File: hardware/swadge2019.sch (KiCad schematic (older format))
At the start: 48 parts, among them P1 PGM, P10 CONN_1, P11 CONN_1, P12 CONN_1, P13 CONN_1, P2 USBMicroB-10118192-0001LF, P3 SAO, P4 CONN_1, P6 CONN_1, P7 CONN_1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

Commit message: update design
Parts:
- C1: value 10u -> 22u
- R11, R9: value 1.5k -> NP_1k
- R3: value 22k -> 10k
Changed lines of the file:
@@
 P 7000 3150
 F 0 "C1" H 7025 3250 50  0000 L CNN
-F 1 "10u" H 7025 3050 50  0000 L CNN
+F 1 "22u" H 7025 3050 50  0000 L CNN
 F 2 "C_0805" H 7038 3000 50  0000 C CNN
 F 3 "" H 7000 3150 50  0000 C CNN
@@
 P 1700 2050
 F 0 "R3" V 1780 2050 50  0000 C CNN
-F 1 "22k" V 1700 2050 50  0000 C CNN
+F 1 "10k" V 1700 2050 50  0000 C CNN
 F 2 "R_0805" V 1630 2050 50  0000 C CNN
 F 3 "" H 1700 2050 50  0000 C CNN
@@
 P 6650 3800
 F 0 "R9" V 6730 3800 50  0000 C CNN
-F 1 "1.5k" V 6650 3800 50  0000 C CNN
+F 1 "NP_1k" V 6650 3800 50  0000 C CNN
 F 2 "R_0805" V 6580 3800 50  0000 C CNN
 F 3 "" H 6650 3800 50  0000 C CNN
@@
 P 7000 3800
 F 0 "R11" V 7080 3800 50  0000 C CNN
-F 1 "1.5k" V 7000 3800 50  0000 C CNN
+F 1 "NP_1k" V 7000 3800 50  0000 C CNN
 F 2 "R_0805" V 6930 3800 50  0000 C CNN
 F 3 "" H 7000 3800 50  0000 C CNN

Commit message: Add RevD
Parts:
- C2: value 1u -> .22u
- C4, C5, C6, C7, C8: value .1u -> .22u
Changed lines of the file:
@@
 P 1050 2350
 F 0 "C2" H 1075 2450 50  0000 L CNN
-F 1 "1u" H 1075 2250 50  0000 L CNN
+F 1 ".22u" H 1075 2250 50  0000 L CNN
 F 2 "C_0805" H 1088 2200 50  0000 C CNN
 F 3 "" H 1050 2350 50  0000 C CNN
@@
 P 7350 3150
 F 0 "C4" H 7375 3250 50  0000 L CNN
-F 1 ".1u" H 7375 3050 50  0000 L CNN
+F 1 ".22u" H 7375 3050 50  0000 L CNN
 F 2 "C_0805" H 7388 3000 50  0000 C CNN
 F 3 "" H 7350 3150 50  0000 C CNN
@@
 P 7750 3150
 F 0 "C5" H 7775 3250 50  0000 L CNN
-F 1 ".1u" H 7775 3050 50  0000 L CNN
+F 1 ".22u" H 7775 3050 50  0000 L CNN
 F 2 "C_0805" H 7788 3000 50  0000 C CNN
 F 3 "" H 7750 3150 50  0000 C CNN
@@
 P 6550 3150
 F 0 "C6" H 6575 3250 50  0000 L CNN
-F 1 ".1u" H 6575 3050 50  0000 L CNN
+F 1 ".22u" H 6575 3050 50  0000 L CNN
 F 2 "C_0805" H 6588 3000 50  0000 C CNN
 F 3 "" H 6550 3150 50  0000 C CNN
@@
 P 1250 3050
 F 0 "C7" H 1275 3150 50  0000 L CNN
-F 1 ".1u" H 1275 2950 50  0000 L CNN
+F 1 ".22u" H 1275 2950 50  0000 L CNN
 F 2 "C_0805" H 1288 2900 50  0000 C CNN
 F 3 "" H 1250 3050 50  0000 C CNN
@@
 P 8050 2550
 F 0 "C8" H 8075 2650 50  0000 L CNN
-F 1 ".1u" H 8075 2450 50  0000 L CNN
+F 1 ".22u" H 8075 2450 50  0000 L CNN
 F 2 "C_0805" H 8088 2400 50  0000 C CNN
 F 3 "" H 8050 2550 50  0000 C CNN

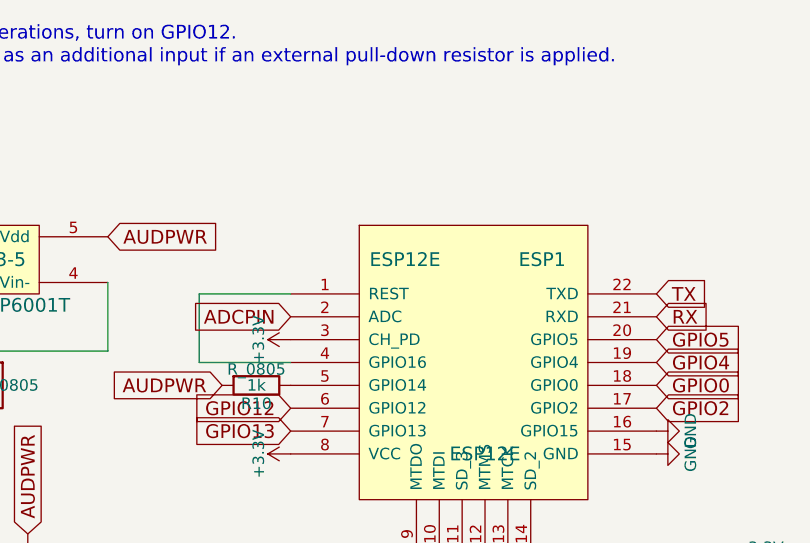
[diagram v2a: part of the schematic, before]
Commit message: Update labels and RFQ
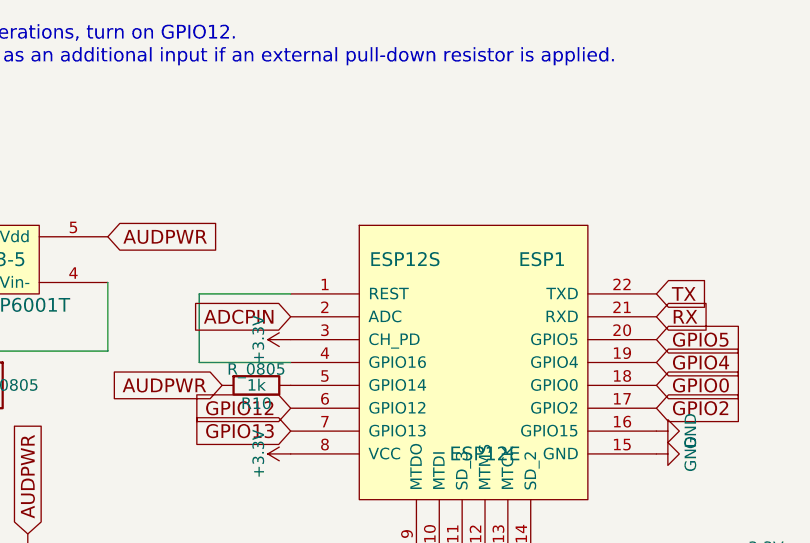
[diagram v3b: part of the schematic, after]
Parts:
- BT1, BT2: MFG (none) -> Use through-hole AA Battery Holder in Style of Keystone 2460
- D3: MFG (none) -> MUST use OFFICIAL SK6812-SIDE LEDs.
- ESP1: value ESP12E -> ESP12S; MFG (none) -> N/A Use ESP12S or ESP12F Modules from Electrodragon
- P2: MFG (none) -> Must use micro USB SMT-only Header, like 10118192-0001LF
- P3: MFG (none) -> Do not populate
- R11, R2, R9: MFG (none) -> Do Not Populate
- SW2: MFG (none) -> Use standard SMT box tactile buttons. Similar to PTS645SM43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
- SW3: Digikey https://www.aliexpress.com/item/50pcs-lot-SMT-3x6x2-5MM-2PI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 -> (none); MFG (none) -> https://www.aliexpress.com/item/50pcs-lot-SMT-3x6x2-5MM-2PI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
- SW7: Cost100 0.48010 -> (none); Digikey 401-1999-6-ND -> (none); MFG (none) -> Use SPDT SLID Switch, like 401-1999-6-ND
- U1: MFG (none) -> Must use MCP6001T Opamp
- U2: MFG (none) -> Use any 1117 3.3V SOT-223 regulator. I.e. AZ1117 or AP1117
- Y1: MFG (none) -> Use a standard through-hole electret microphone.
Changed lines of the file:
@@
 P 3950 2250
 F 0 "ESP1" H 4250 2850 60  0000 C CNN
-F 1 "ESP12E" H 3650 2850 60  0000 C CNN
+F 1 "ESP12S" H 3650 2850 60  0000 C CNN
 F 2 "ESP12E" H 4000 2000 60  0000 C CNN
 F 3 "" H 4000 2000 60  0000 C CNN
+F 4 "N/A Use ESP12S or ESP12F Modules from Electrodragon" H 3950 2250 60  0001 C CNN "MFG"
 	1    3950 2250
 	1    0    0    -1
@@
 F 2 "TACTILE10" H 7350 2100 60  0000 C CNN
 F 3 "" H 7350 2100 60  0000 C CNN
+F 4 "Use standard SMT box tactile buttons.  Similar to PTS645SM43SMTR92. Use RoHS if possible." H 7350 2100 60  0001 C CNN "MFG"
 	1    7350 2100
 	1    0    0    -1
@@
 F 2 "SOT-23-5" H 1800 1650 60  0000 C CNN
 F 3 "" H 1800 1650 60  0000 C CNN
+F 4 "Must use MCP6001T Opamp" H 1800 1650 60  0001 C CNN "MFG"
 	1    1800 1650
 	1    0    0    -1
@@
 F 2 "C_Radial_D8_L13_P3.8" H 700 2550 50  0000 C CNN
 F 3 "" H 800 2800 50  0000 C CNN
+F 4 "Use a standard through-hole electret microphone." H 800 2800 60  0001 C CNN "MFG"
 	1    800  2800
 	0    1    1    0
@@
 F 2 "R_0805" V 5730 3200 50  0000 C CNN
 F 3 "" H 5800 3200 50  0000 C CNN
+F 4 "Do Not Populate" V 5800 3200 60  0001 C CNN "MFG"
 	1    5800 3200
 	1    0    0    -1
@@
 F 2 "SK6812SIDE" H 4700 5350 60  0000 C CNN
 F 3 "" H 4700 5350 60  0000 C CNN
+F 4 "MUST use OFFICIAL SK6812-SIDE LEDs.  " H 4700 5350 60  0001 C CNN "MFG"
 	1    4700 5350
 	1    0    0    -1
@@
 F 2 "USBMicroB-10118192-0001LF" H 7650 4550 60  0001 C CNN
 F 3 "" H 7650 4550 60  0001 C CNN
+F 4 "Must use micro USB SMT-only Header, like 10118192-0001LF" H 7650 4500 60  0001 C CNN "MFG"
 	1    7650 4500
 	1    0    0    -1
@@
 F 2 "JS_SWITCH" H 8800 3300 50  0000 C CNN
 F 3 "" H 8800 3300 50  0000 C CNN
-F 4 "401-1999-6-ND" H 8800 3300 60  0001 C CNN "Digikey"
-F 5 "0.48010" H 8800 3300 60  0001 C CNN "Cost100"
+F 4 "Use SPDT SLID Switch, like 401-1999-6-ND" H 8800 3300 60  0001 C CNN "MFG"
 	1    8800 3300
 	1    0    0    -1
@@
 F 2 "SOT-223" H 9350 4350 60  0000 C CNN
 F 3 "" H 9350 4350 60  0000 C CNN
+F 4 "Use any 1117 3.3V SOT-223 regulator.  I.e. AZ1117 or AP1117" H 9350 4350 60  0001 C CNN "MFG"
 	1    9350 4350
 	1    0    0    -1
@@
 F 2 "BCAAPC" V 10050 3040 50  0000 C CNN
 F 3 "" V 10050 3040 50  0000 C CNN
+F 4 "Use through-hole AA Battery Holder in Style of Keystone 2460" H 10050 3000 60  0001 C CNN "MFG"
 	1    10050 3000
 	1    0    0    -1
@@
 F 2 "BCAAPC" V 10050 3340 50  0000 C CNN
 F 3 "" V 10050 3340 50  0000 C CNN
+F 4 "Use through-hole AA Battery Holder in Style of Keystone 2460" H 10050 3300 60  0001 C CNN "MFG"
 	1    10050 3300
 	1    0    0    -1
@@
 F 2 "R_0805" V 6580 3800 50  0000 C CNN
 F 3 "" H 6650 3800 50  0000 C CNN
+F 4 "Do Not Populate" V 6650 3800 60  0001 C CNN "MFG"
 	1    6650 3800
 	1    0    0    -1
@@
 F 2 "Pin_Header_Straight_2x02" H 7500 5100 50  0000 C CNN
 F 3 "" H 7500 4150 50  0000 C CNN
+F 4 "Do not populate" H 7500 5350 60  0001 C CNN "MFG"
 	1    7500 5350
 	1    0    0    -1
@@
 F 2 "R_0805" V 6930 3800 50  0000 C CNN
 F 3 "" H 7000 3800 50  0000 C CNN
+F 4 "Do Not Populate" V 7000 3800 60  0001 C CNN "MFG"
 	1    7000 3800
 	1    0    0    -1
@@
 F 2 "TACT_3x6_SINGLE" H 7400 1150 50  0000 C CNN
 F 3 "" H 7400 1150 50  0000 C CNN
-F 4 "https://www.aliexpress.com/item/50pcs-lot-SMT-3x6x2-5MM-2PIN-Tactile-Tact-Push-Button-Micro-Switch-G73-Self-reset-Momentary/32804523270.html?spm=2114.search0104.3.65.6bbc193exM3dfC&ws_ab_test=searchweb0_0,searchweb201602_3_10065_10068_10130_318_10547_319_10546_317_10548_10545_10696_450_10084_10083_10618_452_535_534_533_10307_532_204_10059_10884_10887_100031_320_10103_448_449,searchweb201603_60,ppcSwitch_0&algo_expid=b407050b-5903-45ff-9783-15a47ce9142d-9&algo_pvid=b407050b-5903-45ff-9783-15a47ce9142d&priceBeautifyAB=0" H 7400 1150 60  0001 C CNN "Digikey"
+F 4 "https://www.aliexpress.com/item/50pcs-lot-SMT-3x6x2-5MM-2PIN-Tactile-Tact-Push-Button-Micro-Switch-G73-Self-reset-Momentary/32804523270.html?spm=2114.search0104.3.65.6bbc193exM3dfC&ws_ab_test=searchweb0_0,searchweb201602_3_10065_10068_10130_318_10547_319_10546_317_10548_10545_10696_450_10084_10083_10618_452_535_534_533_10307_532_204_10059_10884_10887_100031_320_10103_448_449,searchweb201603_60,ppcSwitch_0&algo_expid=b407050b-5903-45ff-9783-15a47ce9142d-9&algo_pvid=b407050b-5903-45ff-9783-15a47ce9142d&priceBeautifyAB=0" H 7400 1150 60  0001 C CNN "MFG"
 	1    7400 1150
 	1    0    0    -1

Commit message: Update rev with better microphone support
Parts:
- added Y2: Mic, 6mmELECTRET_MIC_SMT, symbol Crystal
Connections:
- net GND: now also Y2.2
- net at C2.2, R6.2, Y1.1: now also Y2.1
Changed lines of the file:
@@
 $EndComp
 $Comp
-L GND #PWR52
+L GND #PWR53
 U 1 1 5B9496E7
 P 3450 5500
-F 0 "#PWR52" H 3450 5250 50  0001 C CNN
+F 0 "#PWR53" H 3450 5250 50  0001 C CNN
 F 1 "GND" H 3450 5350 50  0000 C CNN
 F 2 "" H 3450 5500 50  0000 C CNN
@@
 $EndComp
 $Comp
-L GND #PWR53
+L GND #PWR54
 U 1 1 5B9497A7
 P 4500 5500
-F 0 "#PWR53" H 4500 5250 50  0001 C CNN
+F 0 "#PWR54" H 4500 5250 50  0001 C CNN
 F 1 "GND" H 4500 5350 50  0000 C CNN
 F 2 "" H 4500 5500 50  0000 C CNN
@@
 $EndComp
 $Comp
-L GND #PWR58
+L GND #PWR59
 U 1 1 5B94997F
 P 3450 6400
-F 0 "#PWR58" H 3450 6150 50  0001 C CNN
+F 0 "#PWR59" H 3450 6150 50  0001 C CNN
 F 1 "GND" H 3450 6250 50  0000 C CNN
 F 2 "" H 3450 6400 50  0000 C CNN
@@
 $EndComp
 $Comp
-L GND #PWR59
+L GND #PWR60
 U 1 1 5B949991
 P 4500 6400
-F 0 "#PWR59" H 4500 6150 50  0001 C CNN
+F 0 "#PWR60" H 4500 6150 50  0001 C CNN
 F 1 "GND" H 4500 6250 50  0000 C CNN
 F 2 "" H 4500 6400 50  0000 C CNN
@@
 $EndComp
 $Comp
-L GND #PWR51
+L GND #PWR52
 U 1 1 5B949C6D
 P 2500 5500
-F 0 "#PWR51" H 2500 5250 50  0001 C CNN
+F 0 "#PWR52" H 2500 5250 50  0001 C CNN
 F 1 "GND" H 2500 5350 50  0000 C CNN
 F 2 "" H 2500 5500 50  0000 C CNN
@@
 	800  2450 800  2650
 Wire Wire Line
-	800  2550 1050 2550
+	800  2550 1100 2550
 Wire Wire Line
 	1050 2550 1050 2500
@@
 	2100 6300 2500 6300
 $Comp
-L GND #PWR57
+L GND #PWR58
 U 1 1 5B949FA9
 P 2500 6400
-F 0 "#PWR57" H 2500 6150 50  0001 C CNN
+F 0 "#PWR58" H 2500 6150 50  0001 C CNN
 F 1 "GND" H 2500 6250 50  0000 C CNN
 F 2 "" H 2500 6400 50  0000 C CNN
@@
 $EndComp
 $Comp
-L GND #PWR42
+L GND #PWR43
 U 1 1 5B94A9A3
 P 7600 4800
-F 0 "#PWR42" H 7600 4550 50  0001 C CNN
+F 0 "#PWR43" H 7600 4550 50  0001 C CNN
 F 1 "GND" H 7600 4650 50  0000 C CNN
 F 2 "" H 7600 4800 50  0000 C CNN
@@
 $EndComp
 $Comp
-L GND #PWR43
+L GND #PWR44
 U 1 1 5B94AA02
 P 7700 4800
-F 0 "#PWR43" H 7700 4550 50  0001 C CNN
+F 0 "#PWR44" H 7700 4550 50  0001 C CNN
 F 1 "GND" H 7700 4650 50  0000 C CNN
 F 2 "" H 7700 4800 50  0000 C CNN
@@
 $EndComp
 $Comp
-L GND #PWR44
+L GND #PWR45
 U 1 1 5B94AA61
 P 7800 4800
-F 0 "#PWR44" H 7800 4550 50  0001 C CNN
+F 0 "#PWR45" H 7800 4550 50  0001 C CNN
 F 1 "GND" H 7800 4650 50  0000 C CNN
 F 2 "" H 7800 4800 50  0000 C CNN
@@
 $EndComp
 $Comp
-L GND #PWR45
+L GND #PWR46
 U 1 1 5B94AAC0
 P 7900 4800
-F 0 "#PWR45" H 7900 4550 50  0001 C CNN
+F 0 "#PWR46" H 7900 4550 50  0001 C CNN
 F 1 "GND" H 7900 4650 50  0000 C CNN
 F 2 "" H 7900 4800 50  0000 C CNN
@@
 $EndComp
 $Comp
-L GND #PWR41
+L GND #PWR42
 U 1 1 5B94AB1F
 P 7150 4700
-F 0 "#PWR41" H 7150 4450 50  0001 C CNN
+F 0 "#PWR42" H 7150 4450 50  0001 C CNN
 F 1 "GND" H 7150 4550 50  0000 C CNN
 F 2 "" H 7150 4700 50  0000 C CNN
@@
 $EndComp
 $Comp
-L +5V #PWR37
+L +5V #PWR38
 U 1 1 5B94B2D2
 P 7150 4300
-F 0 "#PWR37" H 7150 4150 50  0001 C CNN
+F 0 "#PWR38" H 7150 4150 50  0001 C CNN
 F 1 "+5V" H 7150 4440 50  0000 C CNN
 F 2 "" H 7150 4300 50  0000 C CNN
@@
 $EndComp
 $Comp
-L GND #PWR39
+L GND #PWR40
 U 1 1 5B94BF15
 P 9900 4450
-F 0 "#PWR39" H 9900 4200 50  0001 C CNN
+F 0 "#PWR40" H 9900 4200 50  0001 C CNN
 F 1 "GND" H 9900 4300 50  0000 C CNN
 F 2 "" H 9900 4450 50  0000 C CNN
@@
 $EndComp
 $Comp
-L +3.3V #PWR54
+L +3.3V #PWR55
 U 1 1 5B94C316
 P 2500 6200
-F 0 "#PWR54" H 2500 6050 50  0001 C CNN
+F 0 "#PWR55" H 2500 6050 50  0001 C CNN
 F 1 "+3.3V" H 2500 6340 50  0000 C CNN
 F 2 "" H 2500 6200 50  0000 C CNN
@@
 $EndComp
 $Comp
-L +3.3V #PWR46
+L +3.3V #PWR47
 U 1 1 5B94C4CF
 P 2500 5300
-F 0 "#PWR46" H 2500 5150 50  0001 C CNN
+F 0 "#PWR47" H 2500 5150 50  0001 C CNN
 F 1 "+3.3V" H 2500 5440 50  0000 C CNN
 F 2 "" H 2500 5300 50  0000 C CNN
@@
 $EndComp
 $Comp
-L +3.3V #PWR47
+L +3.3V #PWR48
 U 1 1 5B94CBC4
 P 3450 5300
-F 0 "#PWR47" H 3450 5150 50  0001 C CNN
+F 0 "#PWR48" H 3450 5150 50  0001 C CNN
 F 1 "+3.3V" H 3450 5440 50  0000 C CNN
 F 2 "" H 3450 5300 50  0000 C CNN
@@
 $EndComp
 $Comp
-L +3.3V #PWR55
+L +3.3V #PWR56
 U 1 1 5B94CC29
 P 3450 6200
-F 0 "#PWR55" H 3450 6050 50  0001 C CNN
+F 0 "#PWR56" H 3450 6050 50  0001 C CNN
 F 1 "+3.3V" H 3450 6340 50  0000 C CNN
 F 2 "" H 3450 6200 50  0000 C CNN
@@
 $EndComp
 $Comp
-L +3.3V #PWR56
+L +3.3V #PWR57
 U 1 1 5B94CC8E
 P 4500 6200
-F 0 "#PWR56" H 4500 6050 50  0001 C CNN
+F 0 "#PWR57" H 4500 6050 50  0001 C CNN
 F 1 "+3.3V" H 4500 6340 50  0000 C CNN
 F 2 "" H 4500 6200 50  0000 C CNN
@@
 $EndComp
 $Comp
-L +3.3V #PWR48
+L +3.3V #PWR49
 U 1 1 5B94CCF3
 P 4500 5300
-F 0 "#PWR48" H 4500 5150 50  0001 C CNN
+F 0 "#PWR49" H 4500 5150 50  0001 C CNN
 F 1 "+3.3V" H 4500 5440 50  0000 C CNN
 F 2 "" H 4500 5300 50  0000 C CNN
@@
 $EndComp
 $Comp
-L +5V #PWR36
+L +5V #PWR37
 U 1 1 5B94D2F0
 P 9900 4250
-F 0 "#PWR36" H 9900 4100 50  0001 C CNN
+F 0 "#PWR37" H 9900 4100 50  0001 C CNN
 F 1 "+5V" H 9900 4390 50  0000 C CNN
 F 2 "" H 9900 4250 50  0000 C CNN
@@
 $EndComp
 $Comp
-L GND #PWR32
+L GND #PWR33
 U 1 1 5B94B42A
 P 5650 3750
-F 0 "#PWR32" H 5650 3500 50  0001 C CNN
+F 0 "#PWR33" H 5650 3500 50  0001 C CNN
 F 1 "GND" H 5650 3600 50  0000 C CNN
 F 2 "" H 5650 3750 50  0000 C CNN
@@
 $EndComp
 $Comp
-L GND #PWR33
+L GND #PWR34
 U 1 1 5B94B430
 P 5650 3900
-F 0 "#PWR33" H 5650 3650 50  0001 C CNN
+F 0 "#PWR34" H 5650 3650 50  0001 C CNN
 F 1 "GND" H 5650 3750 50  0000 C CNN
 F 2 "" H 5650 3900 50  0000 C CNN
@@
 $EndComp
 $Comp
-L GND #PWR34
+L GND #PWR35
 U 1 1 5B94B436
 P 5650 4050
-F 0 "#PWR34" H 5650 3800 50  0001 C CNN
+F 0 "#PWR35" H 5650 3800 50  0001 C CNN
 F 1 "GND" H 5650 3900 50  0000 C CNN
 F 2 "" H 5650 4050 50  0000 C CNN
@@
 $EndComp
 $Comp
-L GND #PWR35
+L GND #PWR36
 U 1 1 5B94B43C
 P 5650 4200
-F 0 "#PWR35" H 5650 3950 50  0001 C CNN
+F 0 "#PWR36" H 5650 3950 50  0001 C CNN
 F 1 "GND" H 5650 4050 50  0000 C CNN
 F 2 "" H 5650 4200 50  0000 C CNN
@@
 $EndComp
 $Comp
-L GND #PWR38
+L GND #PWR39
 U 1 1 5B94B52A
 P 5650 4350
-F 0 "#PWR38" H 5650 4100 50  0001 C CNN
+F 0 "#PWR39" H 5650 4100 50  0001 C CNN
 F 1 "GND" H 5650 4200 50  0000 C CNN
 F 2 "" H 5650 4350 50  0000 C CNN
@@
 $EndComp
 $Comp
-L GND #PWR40
+L GND #PWR41
 U 1 1 5B94B530
 P 5650 4500
-F 0 "#PWR40" H 5650 4250 50  0001 C CNN
+F 0 "#PWR41" H 5650 4250 50  0001 C CNN
 F 1 "GND" H 5650 4350 50  0000 C CNN
 F 2 "" H 5650 4500 50  0000 C CNN
@@
 $EndComp
 $Comp
-L GND #PWR29
+L GND #PWR30
 U 1 1 5B94B7AB
 P 4850 3600
-F 0 "#PWR29" H 4850 3350 50  0001 C CNN
+F 0 "#PWR30" H 4850 3350 50  0001 C CNN
 F 1 "GND" H 4850 3450 50  0000 C CNN
 F 2 "" H 4850 3600 50  0000 C CNN
@@
 $EndComp
 $Comp
-L +3.3V #PWR30
+L +3.3V #PWR31
 U 1 1 5B94FABC
 P 6650 3650
-F 0 "#PWR30" H 6650 3500 50  0001 C CNN
+F 0 "#PWR31" H 6650 3500 50  0001 C CNN
 F 1 "+3.3V" H 6650 3790 50  0000 C CNN
 F 2 "" H 6650 3650 50  0000 C CNN
@@
 $EndComp
 $Comp
-L GND #PWR50
+L GND #PWR51
 U 1 1 5BC45215
 P 7750 5300
-F 0 "#PWR50" H 7750 5050 50  0001 C CNN
+F 0 "#PWR51" H 7750 5050 50  0001 C CNN
 F 1 "GND" H 7750 5150 50  0000 C CNN
 F 2 "" H 7750 5300 50  0000 C CNN
@@
 $EndComp
 $Comp
-L +3.3V #PWR49
+L +3.3V #PWR50
 U 1 1 5BC4539E
 P 7250 5300
-F 0 "#PWR49" H 7250 5150 50  0001 C CNN
+F 0 "#PWR50" H 7250 5150 50  0001 C CNN
 F 1 "+3.3V" H 7250 5440 50  0000 C CNN
 F 2 "" H 7250 5300 50  0000 C CNN
@@
 $EndComp
 $Comp
-L +3.3V #PWR31
+L +3.3V #PWR32
 U 1 1 5BC4BC3D
 P 7000 3650
-F 0 "#PWR31" H 7000 3500 50  0001 C CNN
+F 0 "#PWR32" H 7000 3500 50  0001 C CNN
 F 1 "+3.3V" H 7000 3790 50  0000 C CNN
 F 2 "" H 7000 3650 50  0000 C CNN
@@
 	-1   0    0    1
 $EndComp
+$Comp
+L Crystal Y2
+U 1 1 5BD94020
+P 800 3450
+F 0 "Y2" H 800 3600 50  0000 C CNN
+F 1 "Mic" H 800 3300 50  0000 C CNN
+F 2 "6mmELECTRET_MIC_SMT" H 700 3200 50  0000 C CNN
+F 3 "" H 800 3450 50  0000 C CNN
+F 4 "Use a standard through-hole electret microphone." H 800 3450 60  0001 C CNN "MFG"
+	1    800  3450
+	0    1    1    0
+$EndComp
+$Comp
+L GND #PWR29
+U 1 1 5BD94187
+P 800 3600
+F 0 "#PWR29" H 800 3350 50  0001 C CNN
+F 1 "GND" H 800 3450 50  0000 C CNN
+F 2 "" H 800 3600 50  0000 C CNN
+F 3 "" H 800 3600 50  0000 C CNN
+	1    800  3600
+	1    0    0    -1
+$EndComp
+Wire Wire Line
+	800  3300 1100 3300
+Wire Wire Line
+	1100 3300 1100 2550
+Connection ~ 1050 2550
 $EndSCHEMATC

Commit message: Bump rev G gerbers.
Remove SMT mic.

Add new holes for smaller possible mic spacing
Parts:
- removed Y2: Mic, 6mmELECTRET_MIC_SMT, symbol Crystal

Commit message: Update with rev H - fixed SAO
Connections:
- net GND: now also P3.3 (P3); no longer P3.2 (P2)
- net GPIO4: now also P3.2 (P2); no longer P3.3 (P3)
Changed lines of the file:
@@
 L GND #PWR054
 U 1 1 5BC45215
-P 7750 5300
-F 0 "#PWR054" H 7750 5050 50  0001 C CNN
-F 1 "GND" H 7750 5150 50  0000 C CNN
-F 2 "" H 7750 5300 50  0000 C CNN
-F 3 "" H 7750 5300 50  0000 C CNN
-	1    7750 5300
-	0    -1   -1   0
+P 7250 5400
+F 0 "#PWR054" H 7250 5150 50  0001 C CNN
+F 1 "GND" H 7250 5250 50  0000 C CNN
+F 2 "" H 7250 5400 50  0000 C CNN
+F 3 "" H 7250 5400 50  0000 C CNN
+	1    7250 5400
+	0    1    1    0
 $EndComp
 $Comp
@@
 Text GLabel 7050 2000 0    60   Input ~ 0
 GPIO13
-Text GLabel 7250 5400 0    60   Input ~ 0
+Text GLabel 7750 5300 2    60   Input ~ 0
 GPIO4
 Text GLabel 6650 3950 0    60   Input ~ 0
